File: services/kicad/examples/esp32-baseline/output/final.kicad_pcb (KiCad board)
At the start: 2 copper layers, 93.1 x 69.8 mm, 20 parts, among them J1 5V, U1 ESP32-WROOM-32, U2 AMS1117-3.3

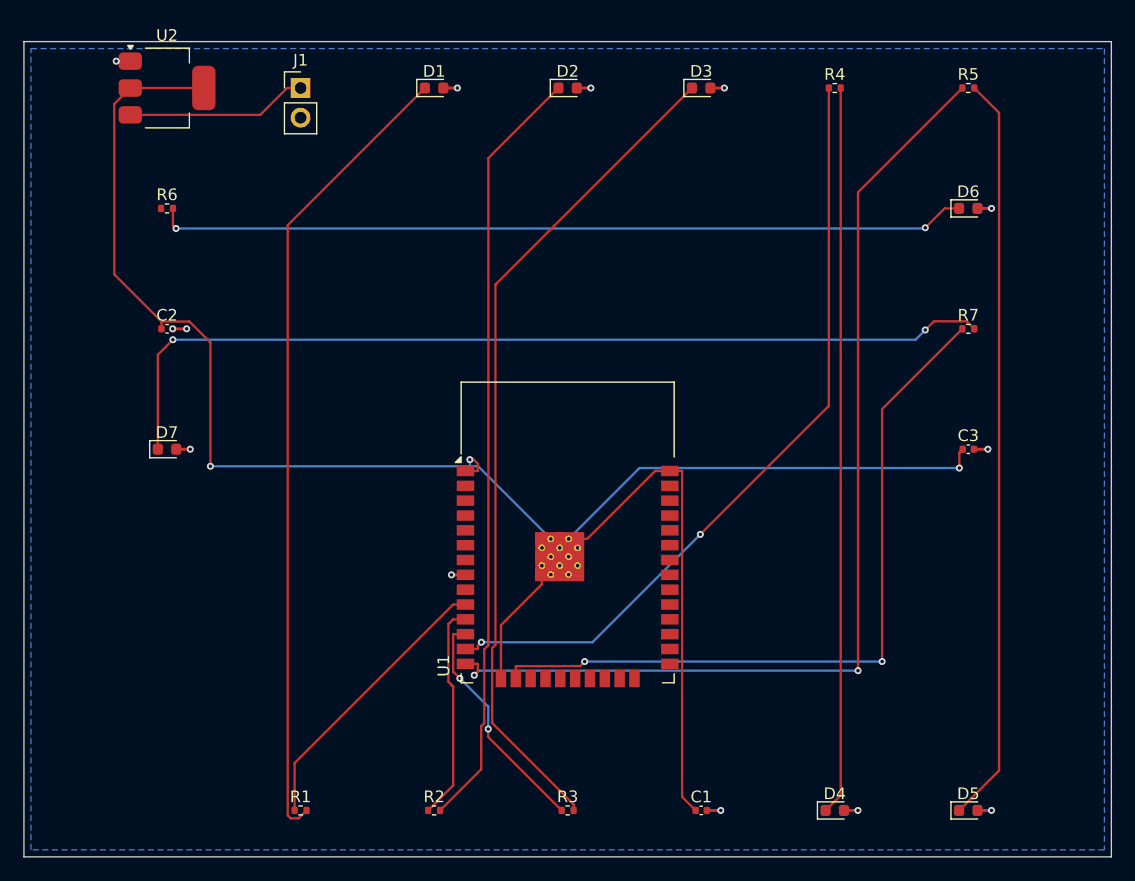
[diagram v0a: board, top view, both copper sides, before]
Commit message: feat(kicad): placement pro et routage 100 % fabricable sur les 16 cartes -- integration sur main (#164)
Branche d'integration coupee depuis origin/main (fab2a82, PR #162) : les
fichiers cles de main etaient des instantanes de feat/placement-seed-snap-
bypass (routing.py = 7981019, placement.py = 437a8b4...). On reprend donc
l'arbre entier de cette branche (345 commits, dernier 9f48667) et on y
conserve ce que main seul apportait :
- tools/verrou_routage.py + son test : « 6,2 Go par routage » rectifie
  (0,2 Go mesure ; c'est la concurrence qui emballe la memoire) ;
- tests/test_driver_llm_resync.py ;
- CLAUDE.md, PLAN.md, DECISIONS.md : fusion a trois voies, les sections
  des deux lignes conservees (2026-09-05 conteneur/verrou, 2026-09-07
  parcours asynchrone et chaine du driver, 2026-09-09/10 lecons).
Les skills *-delegate restent supprimes (remplaces le 2026-08-30).

Contenu : banc en deux phases (placement valide puis routage gele), snap
sur les regles natives, repli GND cible, journal Freerouting incremental,
horloge sans progres, via d'echappement vers le plan principal,
serigraphie degagee ; 16 cartes livrees a 100 %, 0 erreur DRC.

Verification : pytest services/kicad 1805 passed, 16 skipped ;
pnpm type-check 8/8.


Claude-Session: https://claude.ai/code/session_01TnMqm4La2CxQHHB5K8aSSV

Co-authored-by: Claude Fable 5.1 <noreply@anthropic.com>
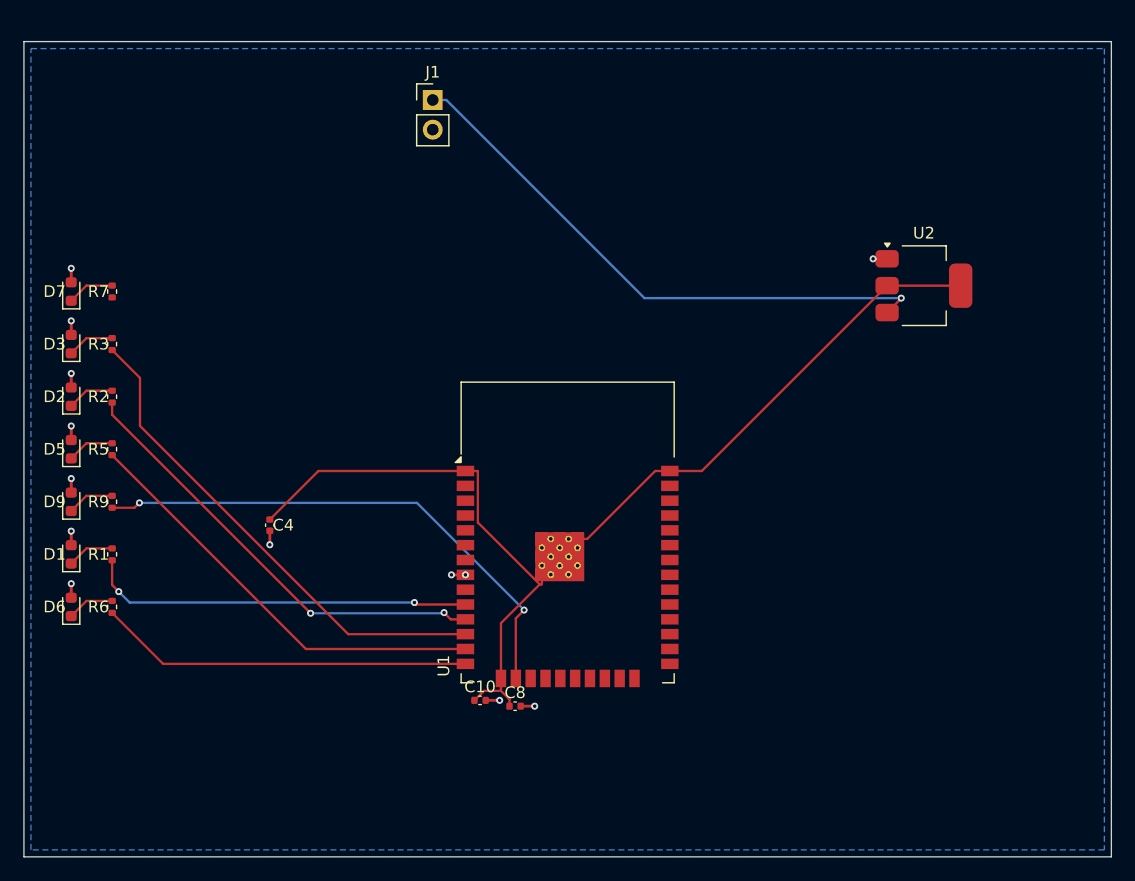
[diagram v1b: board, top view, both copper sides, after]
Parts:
- removed C1, C2, C3: 100nF, C_0402_1005Metric
- removed D4: LED, LED_0603_1608Metric
- removed R4: 330, R_0402_1005Metric
- added C10: 100nF, C_0402_1005Metric, F.Cu at (141.0, 126.5)
- added C4: 100nF, C_0402_1005Metric, F.Cu at (123.0, 111.5)
- added C8: 100nF, C_0402_1005Metric, F.Cu at (144.0, 127.0)
- added D9: LED, LED_0603_1608Metric, F.Cu at (106.0, 109.5)
- added R9: 330, R_0402_1005Metric, F.Cu at (109.5, 109.5)
- moved D6 84.0 mm to (106.0, 118.5), turned to 90 degrees
- moved D5 82.8 mm to (106.0, 105.0), turned to 90 degrees
- moved R5 79.6 mm to (109.5, 105.0), turned to 90 degrees
- moved R7 73.4 mm to (109.5, 91.5), turned to 90 degrees
- moved U2 67.0 mm to (179.0, 91.0)
- moved D3 58.2 mm to (106.0, 96.0), turned to 90 degrees
- moved R3 55.8 mm to (109.5, 96.0), turned to 90 degrees
- moved D1 50.6 mm to (106.0, 114.0), turned to 90 degrees
- moved D2 50.0 mm to (106.0, 100.5), turned to 90 degrees
- moved R2 44.9 mm to (109.5, 100.5), turned to 90 degrees
- moved R6 34.4 mm to (109.5, 118.5), turned to 90 degrees
- moved R1 27.2 mm to (109.5, 114.0), turned to 90 degrees
- moved D7 15.8 mm to (106.0, 91.5), turned to 90 degrees
- moved J1 11.4 mm to (136.9, 75.1)
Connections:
- D5 pad 1: LED6 -> LED5
- D6 pad 1: LED7 -> LED6
- D7 pad 1: LED9 -> LED7
- R5 pad 1: GPIO6 -> GPIO5
- R5 pad 2: LED6 -> LED5
- R6 pad 1: GPIO7 -> GPIO6
- R6 pad 2: LED7 -> LED6
- R7 pad 1: GPIO9 -> GPIO7
- R7 pad 2: LED9 -> LED7
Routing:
- net +3V3: track 187.6 -> 109.0 mm, vias 3 -> 0
- net LED9: track 79.4 -> 4.04 mm, vias 2 -> 0
- net LED3: track 71.8 -> 4.04 mm
- net LED7: track 69.6 -> 4.04 mm, vias 2 -> 0
- net LED1: track 69.1 -> 4.04 mm
- net LED2: track 66.0 -> 4.04 mm
- net LED6: track 64.1 -> 4.04 mm
- net LED5: track 62.4 -> 4.04 mm
- net GPIO6: track 88.8 -> 32.1 mm, vias 2 -> 0
- net VIN: track 15.5 -> 48.9 mm, vias 0 -> 1
- net GPIO5: track 67.1 -> 37.1 mm, vias 2 -> 0
- net GPIO3: track 20.0 -> 42.7 mm, vias 2 -> 0
- net GPIO2: track 18.9 -> 38.6 mm, vias 0 -> 2
- net GPIO9: track 63.9 -> 45.4 mm
- net GPIO1: track 24.3 -> 33.1 mm, vias 0 -> 2
